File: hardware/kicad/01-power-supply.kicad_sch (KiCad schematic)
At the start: 30 parts, among them J1 USB_C, J3 JST PH 2-pin, Q1 SI2301CDS, SW16 SS-12D00G3, U2 IP5306, U3 SY8089AAAC, U4 USBLC6-2SC6

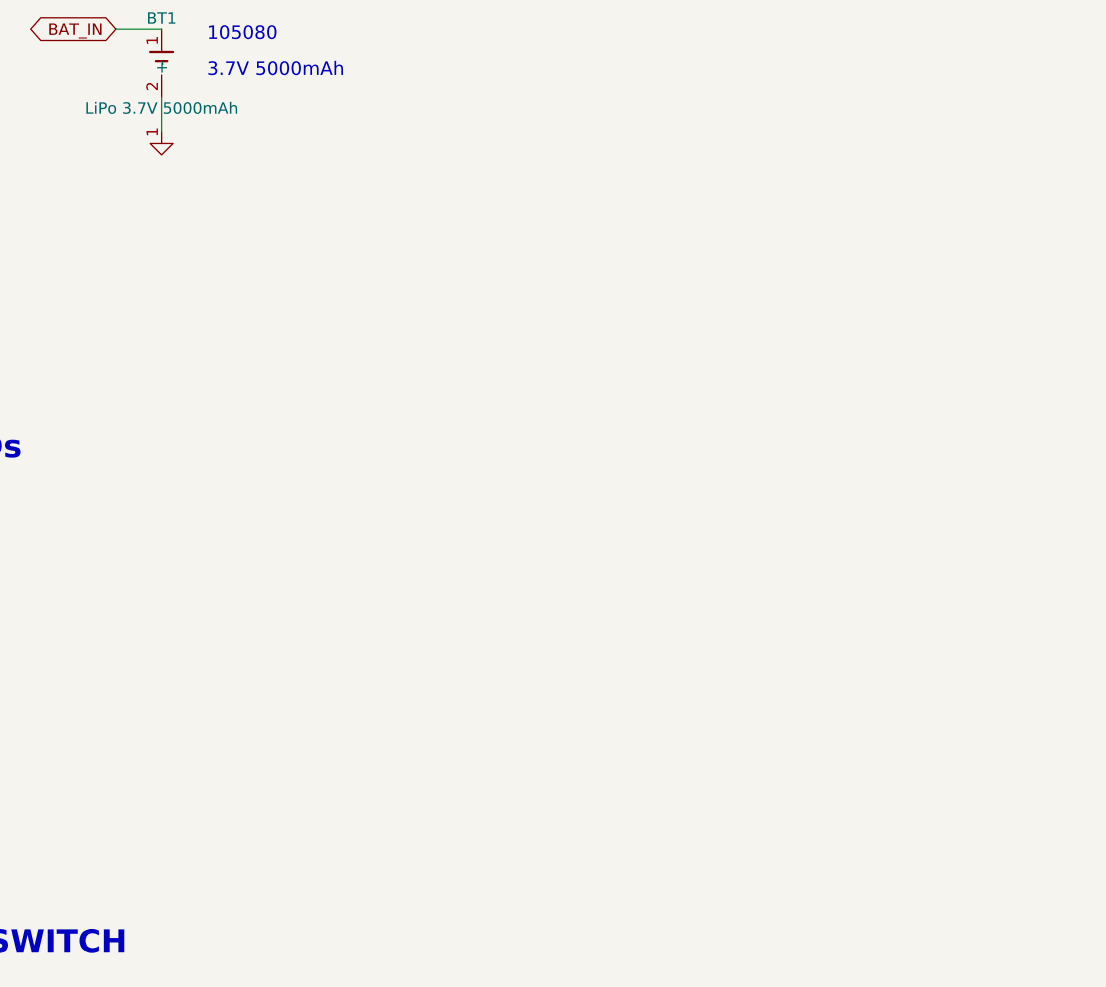
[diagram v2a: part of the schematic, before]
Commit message: feat(diag-leds): two-tier diagnostic LED tree — photo-diagnosable rails + firmware heartbeat
Hardware (workstream H): LED3/R28 on VBUS, LED4/R29 on +5V, LED5/R30 on
+3V3 (passive rail indicators), LED6/R31 on LED_HB (GPIO15 heartbeat) —
all C19171391 red 0805 at ~1 mA, grouped TOP-edge bank silk-labelled
VBUS/5V/3V3/HB, DNP in production. Schematic (power + MCU sheets),
placement, routing, BOM/CPL, datasheet_specs, strict polarity-gate
entries read off the copper.

Firmware (workstream F): LED_HB define in board_config.h (GPIO15,
active HIGH: GPIO -> R31 -> anode, cathode to GND), bringup_test
heartbeat — 1 Hz steady = alive, N blinks + pause = subsystem N failed
(2=SD, 3=display, 4=audio, 5=buttons, 6=PSRAM), BRINGUP-LED telemetry.

Docs: diagnostic-leds roadmap + rework page, first-boot procedure,
bring-up protocol (58 checks), short-test page historical banner.

Also: render_pcba.sh mktemp portability (GNU mktemp needs a XXXXXX
template; BSD accepted the bare -t prefix).

Verification: verify-all 93/93 · verify_dfa 9/9 · injection audit 13/13
fault classes caught · release_jlcpcb synced (incl. nested mirror) +
order-manifest + 13 raytraced renders + repo-map.

Replaces WIP commit 26bc2a0.

Co-Authored-By: Claude Fable 5 <noreply@anthropic.com>
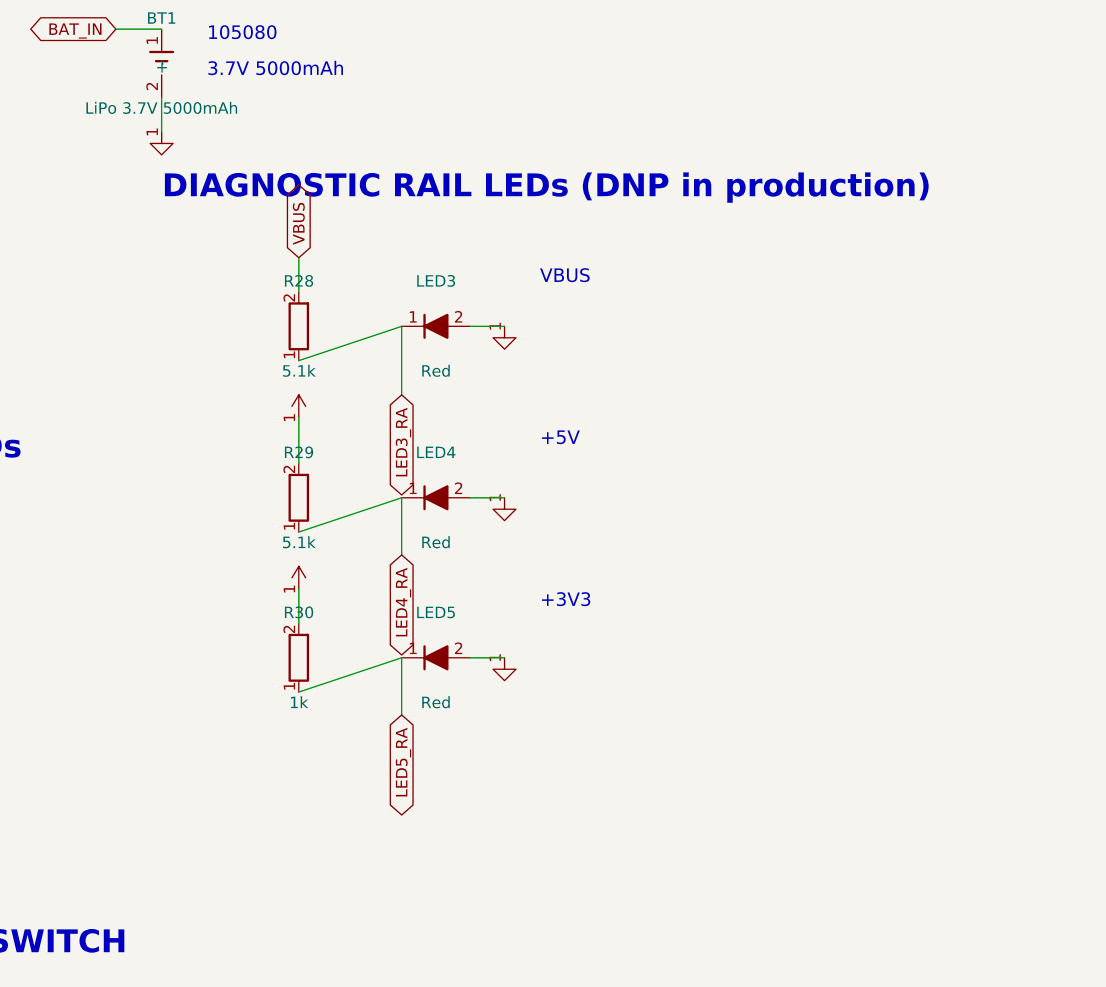
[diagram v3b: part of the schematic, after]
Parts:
- added LED3, LED4, LED5: Red, symbol emu:LED
- added R28, R29: 5.1k, symbol emu:R
- added R30: 1k, symbol emu:R
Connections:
- net +3V3: now also R30.2
- net +5V: now also R29.2
- net GND: now also LED3.2 (K), LED4.2 (K), LED5.2 (K)
- net VBUS: now also R28.2
- new net LED3_RA: LED3.1 (A), R28.1
- new net LED4_RA: LED4.1 (A), R29.1
- new net LED5_RA: LED5.1 (A), R30.1
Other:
- note added: "+3V3"
- note added: "+5V"
- note added: "DIAGNOSTIC RAIL LEDs (DNP in production)"
- note added: "VBUS"
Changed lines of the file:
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@@
   (wire (pts (xy 279.4 162.56) (xy 283.21 162.56)) (stroke (width 0) (type default)))
   (text "Full" (at 287 157 0) (effects (font (size 1.5 1.5)) (justify left)))
+  (text "DIAGNOSTIC RAIL LEDs (DNP in production)" (at 315 104 0) (effects (font (size 2.54 2.54) bold) (justify left)))
+  (symbol (lib_id "emu:R") (at 330.2 119.38 180) (unit 1) (exclude_from_sim no) (in_bom yes) (on_board yes) (dnp no) (property "Reference" "R28" (at 330.2 114.38 0) (effects (font (size 1.27 1.27)))) (property "Value" "5.1k" (at 330.2 124.38 0) (effects (font (size 1.27 1.27)))) (pin "1") (pin "2") (instances (project "esp32-emu-turbo" (path "/00000002-cafe-4000-8000-000000000002" (reference "R28") (unit 1)) (path "/00000001-cafe-4000-8000-000000000001/00000002-cafe-4000-8000-000000000002" (reference "R28") (unit 1)))))
+  (symbol (lib_id "emu:LED") (at 345.44 119.38 0) (unit 1) (exclude_from_sim no) (in_bom yes) (on_board yes) (dnp no) (property "Reference" "LED3" (at 345.44 114.38 0) (effects (font (size 1.27 1.27)))) (property "Value" "Red" (at 345.44 124.38 0) (effects (font (size 1.27 1.27)))) (pin "1") (pin "2") (instances (project "esp32-emu-turbo" (path "/00000002-cafe-4000-8000-000000000002" (reference "LED3") (unit 1)) (path "/00000001-cafe-4000-8000-000000000001/00000002-cafe-4000-8000-000000000002" (reference "LED3") (unit 1)))))
+  (global_label "VBUS" (shape bidirectional) (at 330.2 111.76 90) (effects (font (size 1.27 1.27))) (property "Intersheetrefs" "" (at 0 0 0) (effects (font (size 1.27 1.27)) hide)))
+  (wire (pts (xy 330.2 111.76) (xy 330.2 115.57)) (stroke (width 0) (type default)))
+  (wire (pts (xy 330.2 123.19) (xy 341.63 119.38)) (stroke (width 0) (type default)))
+  (wire (pts (xy 341.63 119.38) (xy 341.63 127.0)) (stroke (width 0) (type default)))
+  (global_label "LED3_RA" (shape bidirectional) (at 341.63 127.0 270) (effects (font (size 1.27 1.27))) (property "Intersheetrefs" "" (at 0 0 0) (effects (font (size 1.27 1.27)) hide)))
+  (symbol (lib_id "emu:GND") (at 353.06 119.38 0) (unit 1) (exclude_from_sim no) (in_bom no) (on_board no) (dnp no) (property "Reference" "#PWR029" (at 353.06 117.38 0) (effects (font (size 1.27 1.27)) hide)) (property "Value" "GND" (at 353.06 121.38 0) (effects (font (size 1.27 1.27)) hide)) (pin "1") (instances (project "esp32-emu-turbo" (path "/00000002-cafe-4000-8000-000000000002" (reference "#PWR029") (unit 1)) (path "/00000001-cafe-4000-8000-000000000001/00000002-cafe-4000-8000-000000000002" (reference "#PWR029") (unit 1)))))
+  (wire (pts (xy 349.25 119.38) (xy 353.06 119.38)) (stroke (width 0) (type default)))
+  (text "VBUS" (at 357 114 0) (effects (font (size 1.5 1.5)) (justify left)))
+  (symbol (lib_id "emu:R") (at 330.2 138.43 180) (unit 1) (exclude_from_sim no) (in_bom yes) (on_board yes) (dnp no) (property "Reference" "R29" (at 330.2 133.43 0) (effects (font (size 1.27 1.27)))) (property "Value" "5.1k" (at 330.2 143.43 0) (effects (font (size 1.27 1.27)))) (pin "1") (pin "2") (instances (project "esp32-emu-turbo" (path "/00000002-cafe-4000-8000-000000000002" (reference "R29") (unit 1)) (path "/00000001-cafe-4000-8000-000000000001/00000002-cafe-4000-8000-000000000002" (reference "R29") (unit 1)))))
+  (symbol (lib_id "emu:LED") (at 345.44 138.43 0) (unit 1) (exclude_from_sim no) (in_bom yes) (on_board yes) (dnp no) (property "Reference" "LED4" (at 345.44 133.43 0) (effects (font (size 1.27 1.27)))) (property "Value" "Red" (at 345.44 143.43 0) (effects (font (size 1.27 1.27)))) (pin "1") (pin "2") (instances (project "esp32-emu-turbo" (path "/00000002-cafe-4000-8000-000000000002" (reference "LED4") (unit 1)) (path "/00000001-cafe-4000-8000-000000000001/00000002-cafe-4000-8000-000000000002" (reference "LED4") (unit 1)))))
+  (symbol (lib_id "emu:+5V") (at 330.2 129.54 0) (unit 1) (exclude_from_sim no) (in_bom no) (on_board no) (dnp no) (property "Reference" "#PWR030" (at 330.2 127.53999999999999 0) (effects (font (size 1.27 1.27)) hide)) (property "Value" "+5V" (at 330.2 131.54 0) (effects (font (size 1.27 1.27)) hide)) (pin "1") (instances (project "esp32-emu-turbo" (path "/00000002-cafe-4000-8000-000000000002" (reference "#PWR030") (unit 1)) (path "/00000001-cafe-4000-8000-000000000001/00000002-cafe-4000-8000-000000000002" (reference "#PWR030") (unit 1)))))
+  (wire (pts (xy 330.2 129.54) (xy 330.2 134.62)) (stroke (width 0) (type default)))
+  (wire (pts (xy 330.2 142.24) (xy 341.63 138.43)) (stroke (width 0) (type default)))
+  (wire (pts (xy 341.63 138.43) (xy 341.63 144.78)) (stroke (width 0) (type default)))
+  (global_label "LED4_RA" (shape bidirectional) (at 341.63 144.78 270) (effects (font (size 1.27 1.27))) (property "Intersheetrefs" "" (at 0 0 0) (effects (font (size 1.27 1.27)) hide)))
+  (symbol (lib_id "emu:GND") (at 353.06 138.43 0) (unit 1) (exclude_from_sim no) (in_bom no) (on_board no) (dnp no) (property "Reference" "#PWR031" (at 353.06 136.43 0) (effects (font (size 1.27 1.27)) hide)) (property "Value" "GND" (at 353.06 140.43 0) (effects (font (size 1.27 1.27)) hide)) (pin "1") (instances (project "esp32-emu-turbo" (path "/00000002-cafe-4000-8000-000000000002" (reference "#PWR031") (unit 1)) (path "/00000001-cafe-4000-8000-000000000001/00000002-cafe-4000-8000-000000000002" (reference "#PWR031") (unit 1)))))
+  (wire (pts (xy 349.25 138.43) (xy 353.06 138.43)) (stroke (width 0) (type default)))
+  (text "+5V" (at 357 132 0) (effects (font (size 1.5 1.5)) (justify left)))
+  (symbol (lib_id "emu:R") (at 330.2 156.21 180) (unit 1) (exclude_from_sim no) (in_bom yes) (on_board yes) (dnp no) (property "Reference" "R30" (at 330.2 151.21 0) (effects (font (size 1.27 1.27)))) (property "Value" "1k" (at 330.2 161.21 0) (effects (font (size 1.27 1.27)))) (pin "1") (pin "2") (instances (project "esp32-emu-turbo" (path "/00000002-cafe-4000-8000-000000000002" (reference "R30") (unit 1)) (path "/00000001-cafe-4000-8000-000000000001/00000002-cafe-4000-8000-000000000002" (reference "R30") (unit 1)))))
+  (symbol (lib_id "emu:LED") (at 345.44 156.21 0) (unit 1) (exclude_from_sim no) (in_bom yes) (on_board yes) (dnp no) (property "Reference" "LED5" (at 345.44 151.21 0) (effects (font (size 1.27 1.27)))) (property "Value" "Red" (at 345.44 161.21 0) (effects (font (size 1.27 1.27)))) (pin "1") (pin "2") (instances (project "esp32-emu-turbo" (path "/00000002-cafe-4000-8000-000000000002" (reference "LED5") (unit 1)) (path "/00000001-cafe-4000-8000-000000000001/00000002-cafe-4000-8000-000000000002" (reference "LED5") (unit 1)))))
+  (symbol (lib_id "emu:+3V3") (at 330.2 148.59 0) (unit 1) (exclude_from_sim no) (in_bom no) (on_board no) (dnp no) (property "Reference" "#PWR032" (at 330.2 146.59 0) (effects (font (size 1.27 1.27)) hide)) (property "Value" "+3V3" (at 330.2 150.59 0) (effects (font (size 1.27 1.27)) hide)) (pin "1") (instances (project "esp32-emu-turbo" (path "/00000002-cafe-4000-8000-000000000002" (reference "#PWR032") (unit 1)) (path "/00000001-cafe-4000-8000-000000000001/00000002-cafe-4000-8000-000000000002" (reference "#PWR032") (unit 1)))))
+  (wire (pts (xy 330.2 148.59) (xy 330.2 152.4)) (stroke (width 0) (type default)))
+  (wire (pts (xy 330.2 160.02) (xy 341.63 156.21)) (stroke (width 0) (type default)))
+  (wire (pts (xy 341.63 156.21) (xy 341.63 162.56)) (stroke (width 0) (type default)))
+  (global_label "LED5_RA" (shape bidirectional) (at 341.63 162.56 270) (effects (font (size 1.27 1.27))) (property "Intersheetrefs" "" (at 0 0 0) (effects (font (size 1.27 1.27)) hide)))
+  (symbol (lib_id "emu:GND") (at 353.06 156.21 0) (unit 1) (exclude_from_sim no) (in_bom no) (on_board no) (dnp no) (property "Reference" "#PWR033" (at 353.06 154.21 0) (effects (font (size 1.27 1.27)) hide)) (property "Value" "GND" (at 353.06 158.21 0) (effects (font (size 1.27 1.27)) hide)) (pin "1") (instances (project "esp32-emu-turbo" (path "/00000002-cafe-4000-8000-000000000002" (reference "#PWR033") (unit 1)) (path "/00000001-cafe-4000-8000-000000000001/00000002-cafe-4000-8000-000000000002" (reference "#PWR033") (unit 1)))))
+  (wire (pts (xy 349.25 156.21) (xy 353.06 156.21)) (stroke (width 0) (type default)))
+  (text "+3V3" (at 357 150 0) (effects (font (size 1.5 1.5)) (justify left)))
   (text "Design Notes:" (at 30 240 0) (effects (font (size 2.54 2.54) bold) (justify left)))
   (text "- IP5306 eSOP-8: integrated charger + synchronous boost (no ext. Schottky)" (at 30 246 0) (effects (font (size 2.54 2.54)) (justify left)))

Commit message: fix(R31): Q1 load-switch orientation + BTN_R off the card-detect pad, audit follow-ups
Hardware-audit round 31 fixes, verified green across all gates before
commit (working set from the parallel audit session, committed on the
user's word to unblock the open-tasks merge):

- R31-HIGH-1: Q1 (SI2301CDS) was in load-switch orientation — the body
  diode conducts on a reversed cell. KiCad placement flipped 0->180 so
  the drain faces the cell; CPL angle back to 90 via the family formula.
  POLARITY_AUDIT Q1 row now records both corrections; vbench Q1 model
  and polarity/design-intent/power-path gates updated.
- R31-HIGH-2: U6 pad 9 is the socket's card-detect spring, not DAT2 —
  a microSD card has eight contacts. BTN_R was copper-merged with a
  switch that grounds it in one card state. BTN_R riser rerouted east of
  the pad row, U6.9 restored to no-net, datasheet_specs corrected.
- R31-MED-3 groundwork, R31-MED-4/LOW doc fixes: MCU sheet GPIO table,
  stale GPIO15/16 comments, schematics.md, net-explorer data.
- retro-go pinned at the R31-HIGH-3/MED-1 sdkconfig fixes.

Co-Authored-By: Claude Fable 5 <noreply@anthropic.com>
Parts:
- removed R17, R18, R30: 1k, symbol emu:R
- removed R25: 100k, symbol emu:R
- removed R28, R29: 5.1k, symbol emu:R
- added LED1, LED2, LED3, LED4, LED5: Red, symbol emu:LED
- added R26: 22k, symbol emu:R
- C29: renamed from R26; value 22k -> 22pF; symbol emu:R -> emu:C
- R17: renamed from LED1; value Red -> 1k; symbol emu:LED -> emu:R
- R18: renamed from LED2; value Red -> 1k; symbol emu:LED -> emu:R
- R25: renamed from C29; value 22pF -> 100k; symbol emu:C -> emu:R
- R28: renamed from LED3; value Red -> 5.1k; symbol emu:LED -> emu:R
- R29: renamed from LED4; value Red -> 5.1k; symbol emu:LED -> emu:R
- R30: renamed from LED5; value Red -> 1k; symbol emu:LED -> emu:R
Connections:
- net +3V3: now also C29.1, R17.2, R18.2, R30.2
- net +5V: now also R29.2
- net BAT+: now also Q1.2; no longer Q1.3
- net BAT_IN: now also Q1.3; no longer Q1.2
- net BUCK_FB: now also C29.2, R26.1; no longer C29.1
- net GND: now also LED1.2 (K), LED2.2 (K), LED3.2 (K), LED4.2 (K), LED5.2 (K), R26.2; no longer C29.2, R17.2 (K), R18.2 (K), R28.2 (K), R29.2 (K), R30.2 (K)
- net LED1_RA: now also LED1.1 (A)
- net LED2_RA: now also LED2.1 (A)
- net LED3_RA: now also LED3.1 (A)
- net LED4_RA: now also LED4.1 (A)
- net LED5_RA: now also LED5.1 (A)
- net VBUS: now also R28.2
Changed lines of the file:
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@@
   (text "(SI2301CDS)" (at 204 80 0) (effects (font (size 1.5 1.5)) (justify left)))
   (wire (pts (xy 190.5 87.63) (xy 199.39 87.63)) (stroke (width 0) (type default)))
-  (wire (pts (xy 199.39 87.63) (xy 209.55 87.63)) (stroke (width 0) (type default)))
   (junction (at 185.42 87.63) (diameter 0) (color 0 0 0 0))
-  (wire (pts (xy 209.55 87.63) (xy 209.55 86.36)) (stroke (width 0) (type default)))
   (global_label "BAT+" (shape bidirectional) (at 199.39 87.63 180) (effects (font (size 1.27 1.27))) (property "Intersheetrefs" "" (at 0 0 0) (effects (font (size 1.27 1.27)) hide)))
-  (wire (pts (xy 214.63 92.71) (xy 214.63 90.17)) (stroke (width 0) (type default)))
-  (wire (pts (xy 214.63 90.17) (xy 241.3 90.17)) (stroke (width 0) (type default)))
+  (wire (pts (xy 209.55 86.36) (xy 209.55 83.82)) (stroke (width 0) (type default)))
+  (wire (pts (xy 209.55 83.82) (xy 226.06 83.82)) (stroke (width 0) (type default)))
+  (global_label "BAT_IN" (shape bidirectional) (at 226.06 83.82 0) (effects (font (size 1.27 1.27))) (property "Intersheetrefs" "" (at 0 0 0) (effects (font (size 1.27 1.27)) hide)))
+  (wire (pts (xy 214.63 92.71) (xy 214.63 101.6)) (stroke (width 0) (type default)))
+  (global_label "BAT+" (shape bidirectional) (at 214.63 101.6 270) (effects (font (size 1.27 1.27))) (property "Intersheetrefs" "" (at 0 0 0) (effects (font (size 1.27 1.27)) hide)))
   (wire (pts (xy 241.3 90.17) (xy 261.62 90.17)) (stroke (width 0) (type default)))
-  (global_label "BAT_IN" (shape bidirectional) (at 241.3 90.17 0) (effects (font (size 1.27 1.27))) (property "Intersheetrefs" "" (at 0 0 0) (effects (font (size 1.27 1.27)) hide)))
+  (global_label "BAT_IN" (shape bidirectional) (at 241.3 90.17 180) (effects (font (size 1.27 1.27))) (property "Intersheetrefs" "" (at 0 0 0) (effects (font (size 1.27 1.27)) hide)))
   (symbol (lib_id "emu:R") (at 201.93 101.6 0) (unit 1) (exclude_from_sim no) (in_bom yes) (on_board yes) (dnp no) (property "Reference" "R24" (at 201.93 96.6 0) (effects (font (size 1.27 1.27)))) (property "Value" "100k" (at 201.93 106.6 0) (effects (font (size 1.27 1.27)))) (pin "1") (pin "2") (instances (project "esp32-emu-turbo" (path "/00000002-cafe-4000-8000-000000000002" (reference "R24") (unit 1)) (path "/00000001-cafe-4000-8000-000000000001/00000002-cafe-4000-8000-000000000002" (reference "R24") (unit 1)))))
   (text "Q1 gate PD" (at 197 116 0) (effects (font (size 1.5 1.5)) (justify left)))
